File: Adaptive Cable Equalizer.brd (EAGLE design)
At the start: 26.3 x 48.3 mm, 37 parts, among them J1 HD-BNC, J2 SMA132357, J3 SMA132357, SW1 219-02J, U1 GS3440

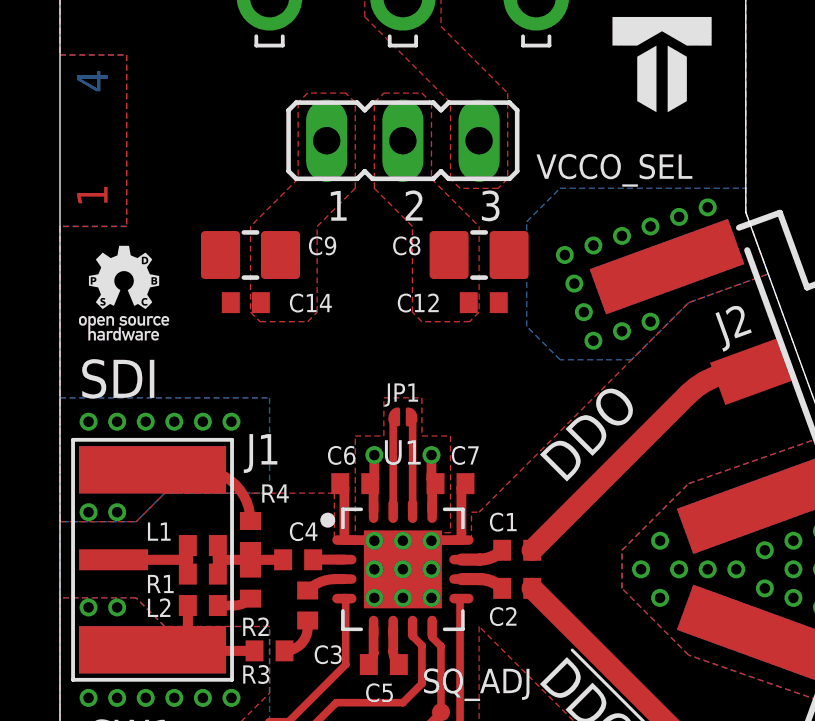
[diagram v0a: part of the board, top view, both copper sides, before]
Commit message: Improved decoupling capacitor placement
+: Added polygons for IC's VCC_A and VCC_O supplies
+: Added multiple vias around distant "bulk" capacitors
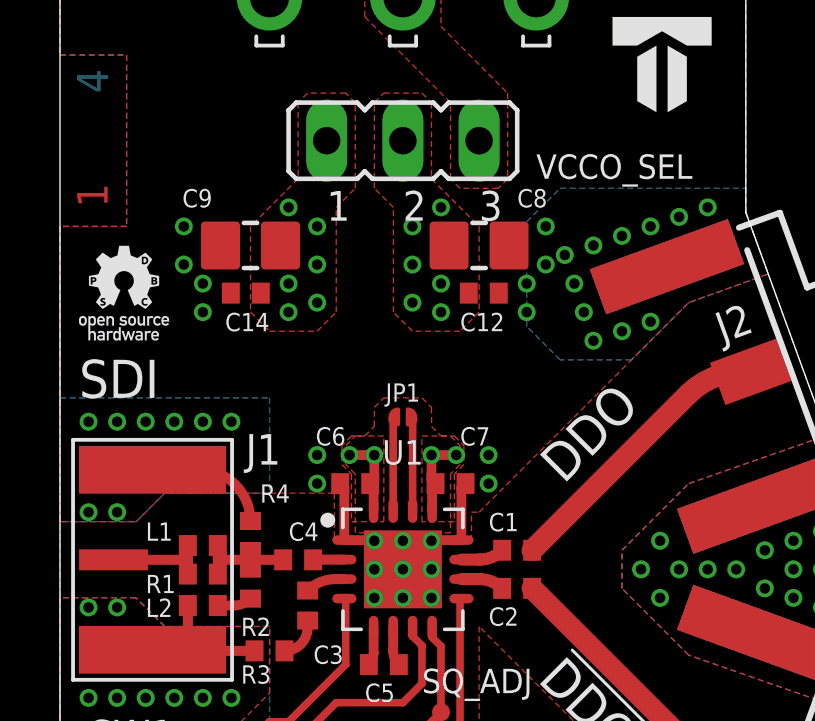
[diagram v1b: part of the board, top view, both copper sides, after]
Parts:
- moved C12 0.32 mm to (14.1, 33.3)
- moved C14 0.32 mm to (6.19, 33.3)
- moved C8 0.32 mm to (14.0, 34.9)
- moved C9 0.32 mm to (6.35, 34.9)
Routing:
- net VDD: track 1.96 -> 2.79 mm, vias 1 -> 8
- net VCC: track 5.09 -> 5.91 mm, vias 4 -> 11
- net GND: vias 61 -> 73
